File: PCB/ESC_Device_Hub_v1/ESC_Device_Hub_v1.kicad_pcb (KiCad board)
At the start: 4 copper layers, 50 x 90 mm, 137 parts, among them J1 Conn_01x04, J10 Conn_01x06, J11 Conn_01x02, J12 Conn_01x02, J13 Conn_01x02, J14 Conn_01x02, J15 Conn_01x02, J16 Conn_01x02, J17 Conn_01x02, J18 Conn_01x02, J19 Conn_01x05, J2 Conn_01x04, J20 Conn_01x01, J21 Conn_01x01, J22 Conn_01x02, J3 Conn_01x04, J4 Conn_01x04, J5 Conn_01x04, J6 Conn_01x04, J7 Conn_01x06, J8 Conn_01x06, J9 Conn_01x06, SW1 SW_Push, SW2 SW_Push, SW3 SW_Coded_SH-7050, U1 ISO1042BQDWVQ1, U10 LM66100DCK, U11 LM66100DCK, U18 USB_Type-C, U2 MCP2562FD-H/MF, U3 IS25LP064D-JLLE, U4 STM32H563RGVx, U6 TLP293, U7 NJM2884U1-33, U8 RFM-0505S, Y1 FC2012SN 32.768K-70NNA0KC0, Y2 XRCGB25M000FFS1AR0

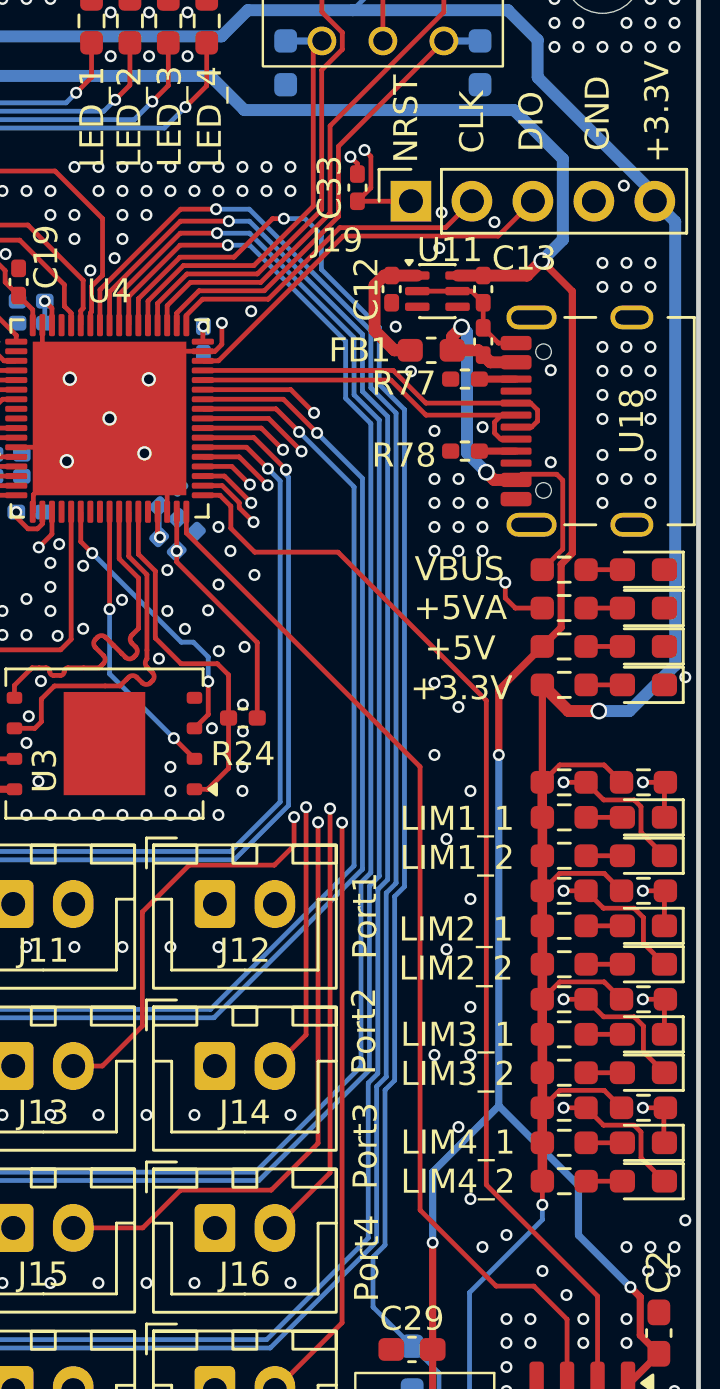
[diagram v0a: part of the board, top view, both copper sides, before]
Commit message: 更にビア追加
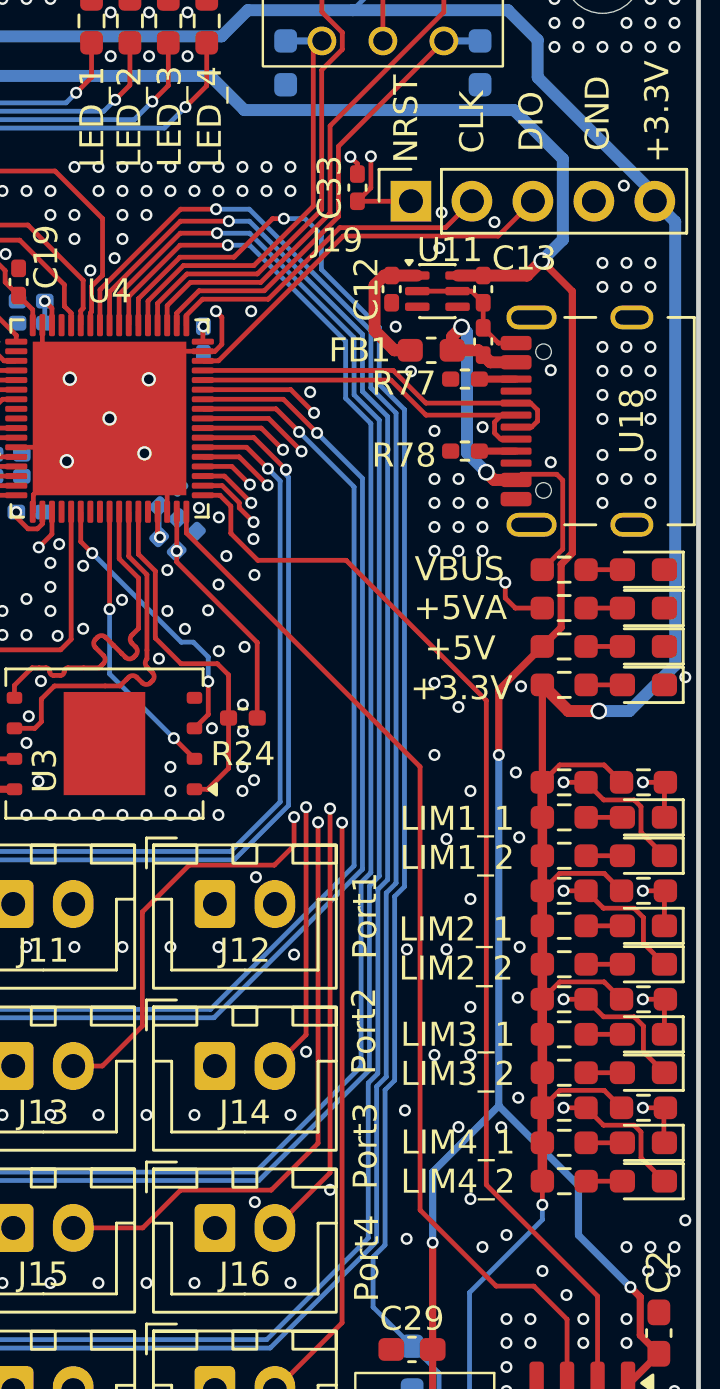
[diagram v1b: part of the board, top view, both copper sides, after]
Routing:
- net GND: track 37.3 -> 37.9 mm, vias 481 -> 500
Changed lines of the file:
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@@
 	)
 	(segment
-		(start 163.806249 50.823751)
-		(end 165.462499 52.48)
+		(start 170.142499 48.263404)
+		(end 170.142499 49.393674)
 		(width 0.2)
 		(layer "F.Cu")
@@
 	)
 	(segment
-		(start 167.09625 50.84625)
+		(start 163.806249 50.823751)
 		(end 165.462499 52.48)
 		(width 0.2)
@@
 	)
 	(segment
-		(start 169.856173 49.68)
-		(end 170.142499 49.393674)
-		(width 0.2)
-		(layer "F.Cu")
-		(net "GND")
-	)
-	(segment
-		(start 170.142499 49.393674)
-		(end 170.142499 48.5)
+		(start 167.09625 50.84625)
+		(end 165.462499 52.48)
 		(width 0.2)
 		(layer "F.Cu")
@@
 	)
 	(segment
+		(start 170.142499 49.393674)
+		(end 169.856173 49.68)
+		(width 0.2)
+		(layer "F.Cu")
+		(net "GND")
+	)
+	(segment
 		(start 167.862499 54.88)
 		(end 166.916249 53.933751)
@@
 	)
 	(segment
-		(start 175.5 41.58)
-		(end 175.79 41.87)
+		(start 169.894162 48.015067)
+		(end 170.142499 48.263404)
 		(width 0.2)
 		(layer "F.Cu")
@@
 	)
 	(segment
-		(start 169.35 49.68)
-		(end 169.856173 49.68)
+		(start 175.5 41.58)
+		(end 175.79 41.87)
 		(width 0.2)
 		(layer "F.Cu")
@@
 	)
 	(segment
+		(start 169.894162 48.01)
+		(end 169.894162 48.015067)
+		(width 0.2)
+		(layer "F.Cu")
+		(net "GND")
+	)
+	(segment
+		(start 169.856173 49.68)
+		(end 169.35 49.68)
+		(width 0.2)
+		(layer "F.Cu")
+		(net "GND")
+	)
+	(segment
 		(start 162.287499 56.3425)
 		(end 162.287499 55.655)
@@
 	)
 	(via
-		(at 170.142499 48.5)
+		(at 169.894162 48.01)
 		(size 0.5)
 		(drill 0.3)
@@
 	)
 	(via
+		(at 171.457696 57.502304)
+		(size 0.5)
+		(drill 0.3)
+		(layers "F.Cu" "B.Cu")
+		(free yes)
+		(net "GND")
+	)
+	(via
 		(at 145 31)
 		(size 0.5)
@@
 	)
 	(via
+		(at 182.39 67.23)
+		(size 0.5)
+		(drill 0.3)
+		(layers "F.Cu" "B.Cu")
+		(free yes)
+		(net "GND")
+	)
+	(via
 		(at 181 57)
 		(size 0.5)
@@
 	)
 	(via
+		(at 173.650001 78.867106)
+		(size 0.5)
+		(drill 0.3)
+		(layers "F.Cu" "B.Cu")
+		(free yes)
+		(net "GND")
+	)
+	(via
 		(at 156 64.5)
 		(size 0.5)
@@
 	)
 	(via
+		(at 174.650001 84.617106)
+		(size 0.5)
+		(drill 0.3)
+		(layers "F.Cu" "B.Cu")
+		(free yes)
+		(net "GND")
+	)
+	(via
 		(at 183.5 88)
 		(size 0.5)
@@
 	)
 	(via
+		(at 182.49 80.78)
+		(size 0.5)
+		(drill 0.3)
+		(layers "F.Cu" "B.Cu")
+		(free yes)
+		(net "GND")
+	)
+	(via
 		(at 163 96)
 		(size 0.5)
@@
 	)
 	(via
+		(at 171.514776 85.129999)
+		(size 0.5)
+		(drill 0.3)
+		(layers "F.Cu" "B.Cu")
+		(free yes)
+		(net "GND")
+	)
+	(via
 		(at 149 31)
 		(size 0.5)
@@
 	)
 	(via
+		(at 173.15 74.817716)
+		(size 0.5)
+		(drill 0.3)
+		(layers "F.Cu" "B.Cu")
+		(free yes)
+		(net "GND")
+	)
+	(via
 		(at 152 77)
 		(size 0.5)
@@
 	)
 	(via
-		(at 170 57)
+		(at 169.187499 56.205)
 		(size 0.5)
 		(drill 0.3)
@@
 	)
 	(via
+		(at 177.84 86.66)
+		(size 0.5)
+		(drill 0.3)
+		(layers "F.Cu" "B.Cu")
+		(free yes)
+		(net "GND")
+	)
+	(via
 		(at 146 32)
 		(size 0.5)
@@
 	)
 	(via
+		(at 171.48 67.55)
+		(size 0.5)
+		(drill 0.3)
+		(layers "F.Cu" "B.Cu")
+		(free yes)
+		(net "GND")
+	)
+	(via
 		(at 187 47)
 		(size 0.5)
@@
 	)
 	(via
+		(at 182.607503 63.640317)
+		(size 0.5)
+		(drill 0.3)
+		(layers "F.Cu" "B.Cu")
+		(free yes)
+		(net "GND")
+	)
+	(via
 		(at 164.9 96)
 		(size 0.5)
@@
 	)
 	(via
-		(at 170.5 58)
+		(at 170.328554 58.211446)
 		(size 0.5)
 		(drill 0.3)
@@
 	)
 	(via
+		(at 177.77 81.31)
+		(size 0.5)
+		(drill 0.3)
+		(layers "F.Cu" "B.Cu")
+		(free yes)
+		(net "GND")
+	)
+	(via
 		(at 145.1 96)
 		(size 0.5)
@@
 	)
 	(via
+		(at 177.85 74.6)
+		(size 0.5)
+		(drill 0.3)
+		(layers "F.Cu" "B.Cu")
+		(free yes)
+		(net "GND")
+	)
+	(via
 		(at 188 36)
 		(size 0.5)
@@
 	)
 	(via
+		(at 181.78 82.01)
+		(size 0.5)
+		(drill 0.3)
+		(layers "F.Cu" "B.Cu")
+		(free yes)
+		(net "GND")
+	)
+	(via
 		(at 165.510001 34.087839)
 		(size 0.5)
@@
 	)
 	(via
+		(at 182.55 74.5)
+		(size 0.5)
+		(drill 0.3)
+		(layers "F.Cu" "B.Cu")
+		(free yes)
+		(net "GND")
+	)
+	(via
 		(at 164 69)
 		(size 0.5)
@@
 	)
 	(via
+		(at 171.561585 71.589999)
+		(size 0.5)
+		(drill 0.3)
+		(layers "F.Cu" "B.Cu")
+		(free yes)
+		(net "GND")
+	)
+	(via
 		(at 169 43)
 		(size 0.5)
@@
 	)
 	(via
+		(at 182.47 76.61)
+		(size 0.5)
+		(drill 0.3)
+		(layers "F.Cu" "B.Cu")
+		(free yes)
+		(net "GND")
+	)
+	(via
 		(at 187 36)
 		(size 0.5)
@@
 	)
 	(via
+		(at 170.016053 56.6)
+		(size 0.5)
+		(drill 0.3)
+		(layers "F.Cu" "B.Cu")
+		(free yes)
+		(net "GND")
+	)
+	(via
 		(at 153 58)
 		(size 0.5)
@@
 	)
 	(via
+		(at 182.53 69.93)
+		(size 0.5)
+		(drill 0.3)
+		(layers "F.Cu" "B.Cu")
+		(free yes)
+		(net "GND")
+	)
+	(via
 		(at 188 46)
 		(size 0.5)
@@
 	)
 	(via
+		(at 173.820681 51.379999)
+		(size 0.5)
+		(drill 0.3)
+		(layers "F.Cu" "B.Cu")
+		(free yes)
+		(net "GND")
+	)
+	(via
 		(at 167.09625 50.84625)
 		(size 0.6)
@@
 	)
 	(segment
-		(start 170.059659 55.68)
-		(end 169.35 55.68)
+		(start 170.516053 57.267768)
+		(end 170.516053 56.136394)
 		(width 0.2)
 		(layer "F.Cu")
@@
 	)
 	(segment
-		(start 174.98 58.05)
-		(end 171.51 58.05)
+		(start 170.059659 55.68)
+		(end 169.35 55.68)
 		(width 0.2)
 		(layer "F.Cu")
@@
 	)
 	(segment
-		(start 171.51 58.05)
-		(end 170.516053 57.056053)
+		(start 175.32 58.39)
+		(end 171.638285 58.39)
 		(width 0.2)
 		(layer "F.Cu")
@@
 	)
 	(segment
-		(start 170.516053 57.056053)
-		(end 170.516053 56.136394)
+		(start 181.16 84.41)
+		(end 181.16 64.23)
 		(width 0.2)
 		(layer "F.Cu")
@@
 	)
 	(segment
-		(start 185.795 89.045)
-		(end 181.16 84.41)
+		(start 171.638285 58.39)
+		(end 170.516053 57.267768)
 		(width 0.2)
 		(layer "F.Cu")
@@
 	)
 	(segment
-		(start 181.16 84.41)
-		(end 181.16 64.23)
+		(start 185.795 89.045)
+		(end 181.16 84.41)
 		(width 0.2)
 		(layer "F.Cu")
@@
 	(segment
 		(start 181.16 64.23)
-		(end 174.98 58.05)
+		(end 175.32 58.39)
 		(width 0.2)
 		(layer "F.Cu")
@@
 	)
 	(segment
-		(start 176.35 42.87)
-		(end 175.79 43.43)
+		(start 176.35 41.560685)
+		(end 176.35 42.87)
 		(width 0.2)
 		(layer "F.Cu")
@@
 	)
 	(segment
-		(start 151.5 39.83)
-		(end 150.94 39.83)
+		(start 176.35 42.87)
+		(end 175.79 43.43)
 		(width 0.2)
 		(layer "F.Cu")
@@
 	)
 	(segment
-		(start 176.35 41.560685)
-		(end 176.35 42.87)
+		(start 151.5 39.83)
+		(end 150.94 39.83)
 		(width 0.2)
 		(layer "F.Cu")
@@
 	)
 	(segment
-		(start 176.084071 41.294756)
-		(end 176.35 41.560685)
-		(width 0.2)
-		(layer "F.Cu")
-		(net "NRST")
-	)
-	(segment
 		(start 160.63 52.38)
 		(end 160.63 52.054746)
@@
 	)
 	(via
-		(at 176.084071 41.294756)
+		(at 176.35 41.560685)
 		(size 0.5)
 		(drill 0.3)
@@
 	)
 	(segment
-		(start 176.084071 41.294756)
-		(end 175.409315 40.62)
+		(start 175.409315 40.62)
+		(end 152.29 40.62)
 		(width 0.2)
 		(layer "In2.Cu")
@@
 	)
 	(segment
-		(start 175.409315 40.62)
-		(end 152.29 40.62)
+		(start 176.35 41.560685)
+		(end 175.409315 40.62)
 		(width 0.2)
 		(layer "In2.Cu")

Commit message: 更新　ビア追加2
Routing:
- net GNDD: vias 219 -> 396
- net GND: vias 500 -> 502

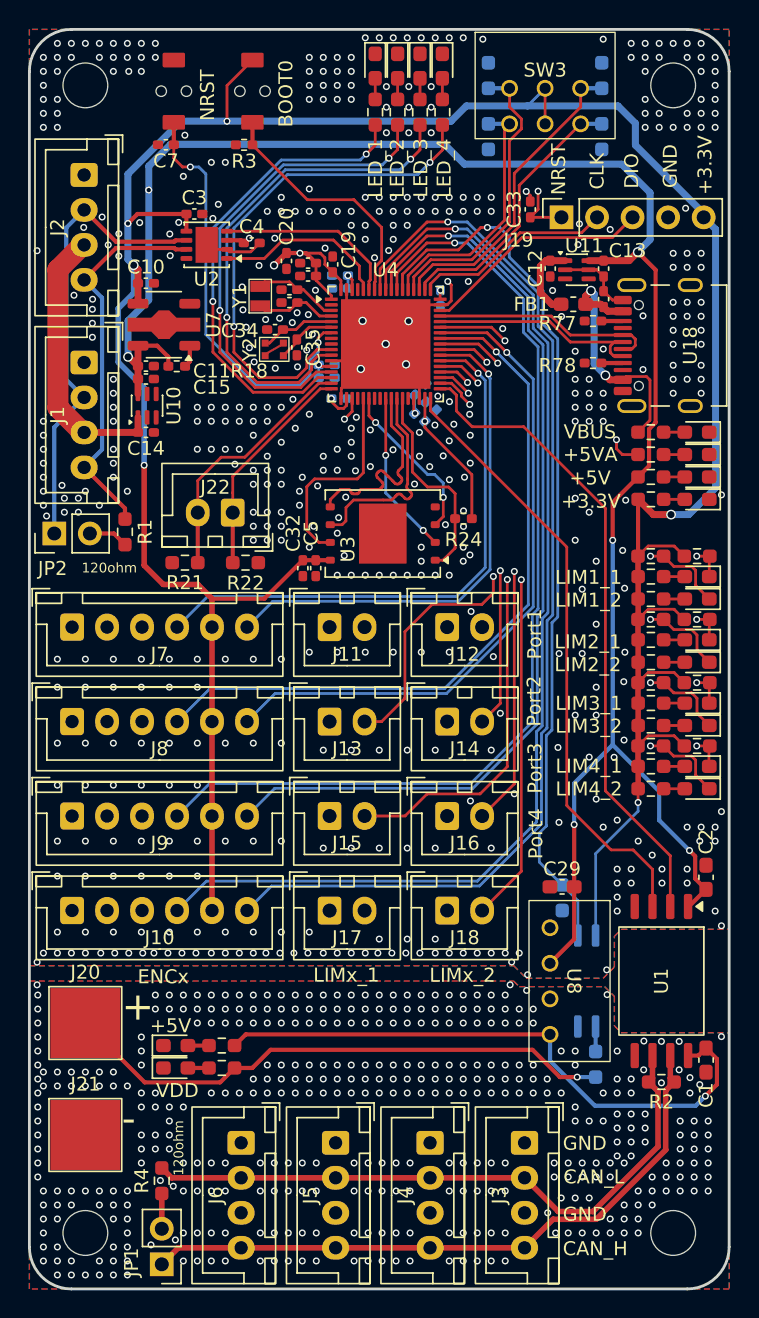
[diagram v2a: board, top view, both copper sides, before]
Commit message: fix:ビアの数を減らした
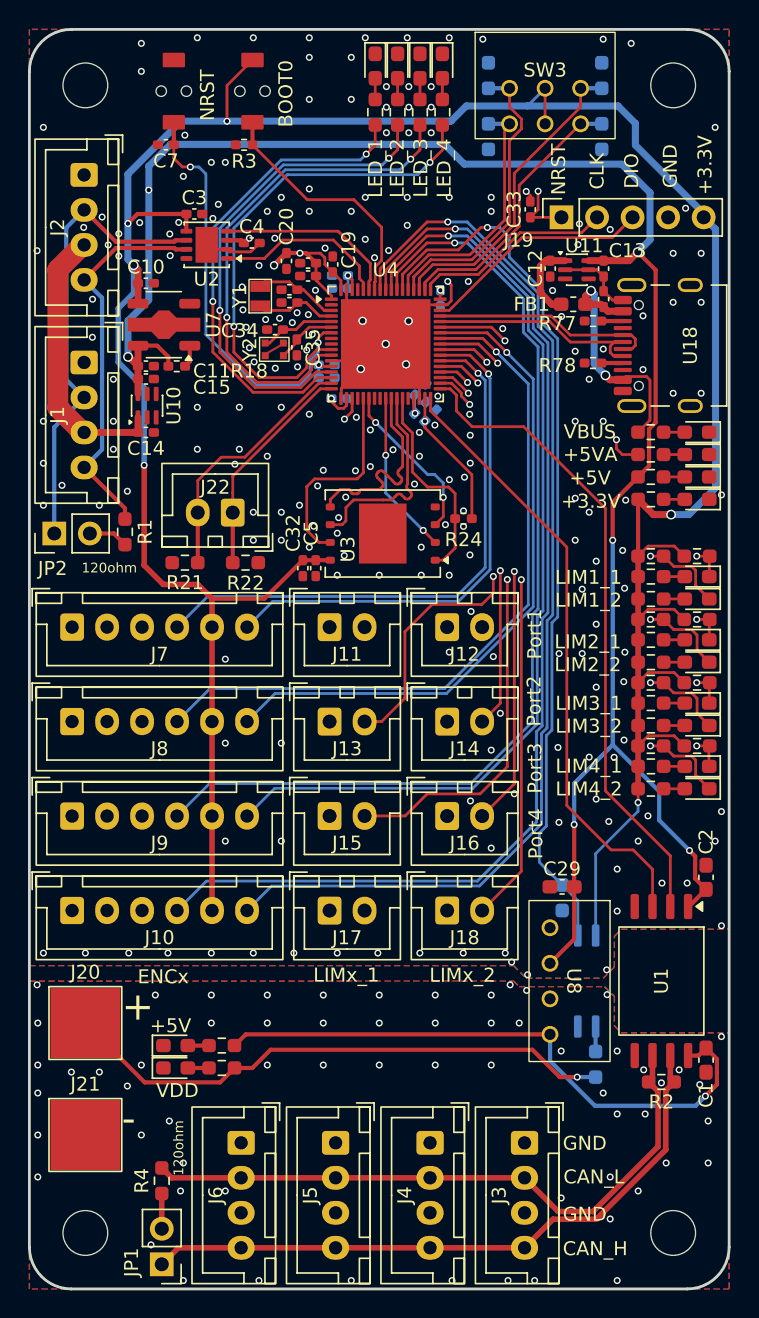
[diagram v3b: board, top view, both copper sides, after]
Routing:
- net GNDD: vias 396 -> 62
- net GND: vias 502 -> 217
